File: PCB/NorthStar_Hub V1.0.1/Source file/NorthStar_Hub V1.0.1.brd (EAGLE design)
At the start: 67 x 37 mm, 187 parts, among them IC1 GL3520-OS322, IC2 ATMEGA32U4-MUR, J1 FH34SRJ-6S-0.5SH(50), J10 NA, J3 FH34SRJ-12S-0.5SH(50), J4 XH-2AW, J5 53398-02, J6 SM04B-SRSS-TB, J9 FH34SRJ-12S-0.5SH(50), K1 SKRKAEE020, Q1 CJ2301 S1, Q2 DTC143ZUA, U1 AT25DF512C-MAHN-T, U2 HD3SS3220IRNHR, U3 GL3224E, U4 SY8089, U5 SY8089, U6 TPS2065C, U7 TPS2065C, U8 TPS2065C, X1 16MHZ, X3 25MHZ, X4 25MHZ

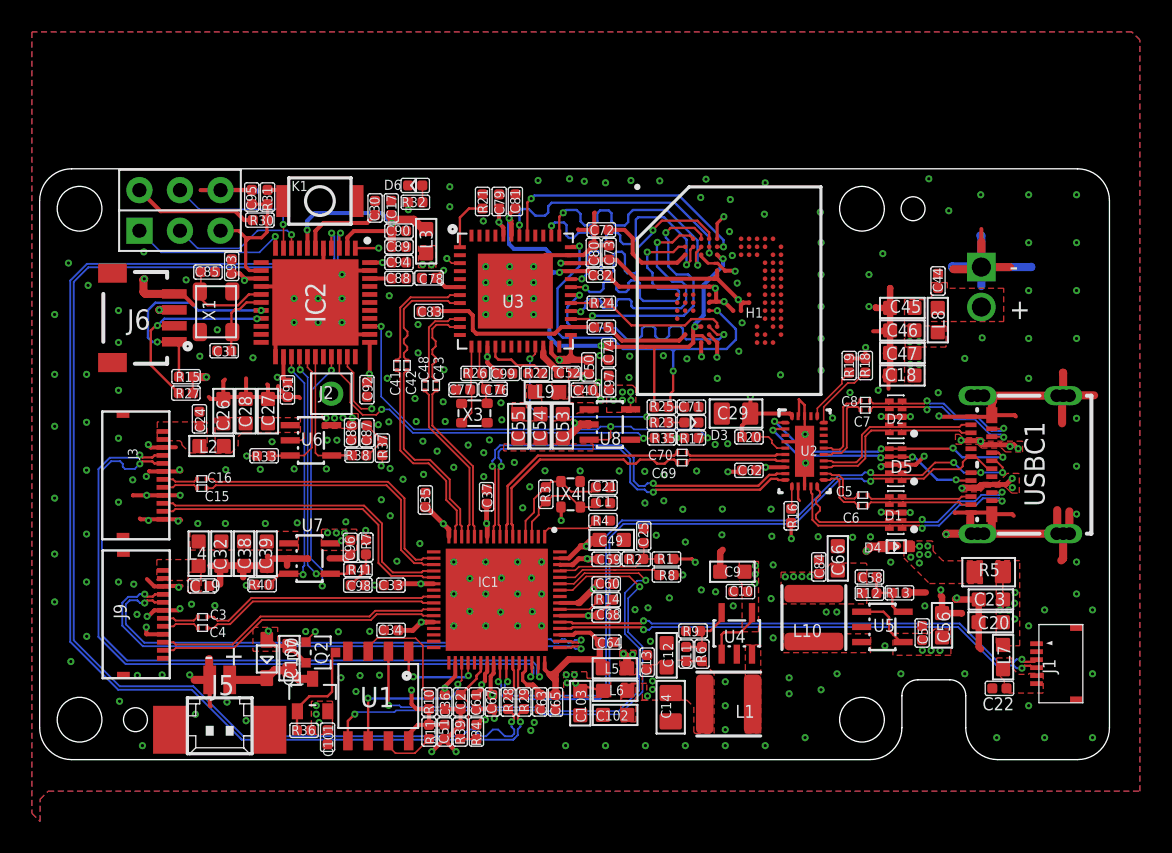
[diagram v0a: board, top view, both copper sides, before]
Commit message: reassign INT to PE6
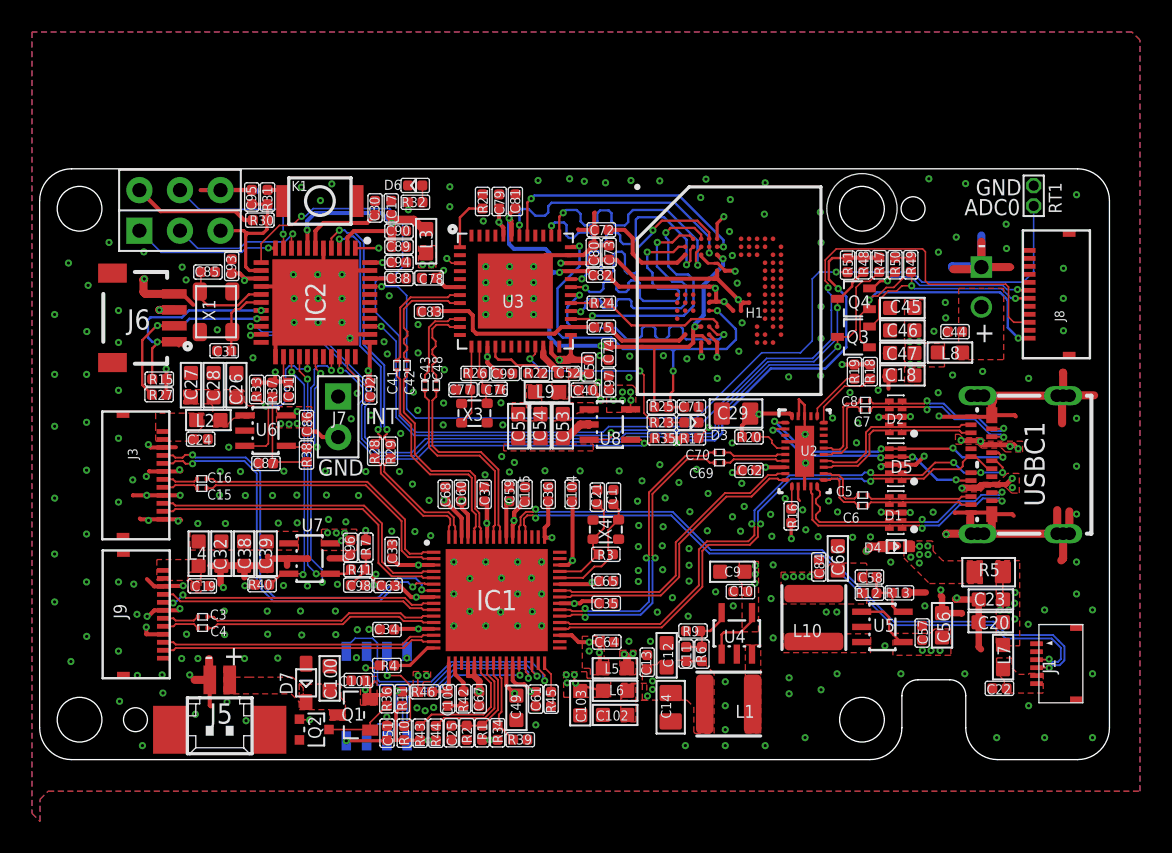
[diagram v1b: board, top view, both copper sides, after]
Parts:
- removed C2: 1uF ±10% 10V, RCL:C0402
- removed J2: (no value), Connector_NOA:1P-60/32MIL
- removed R14: 100K ±1%, RCL:R0402
- removed R8: 10K ±1%, RCL:R0402
- added C104, C105, C106: 100nF ±10% 10V, RCL:C0402
- added J7: 2.54MM 单排正弯针 1*2P PA6.0, Connector_NOA:2P-2.54-65/35MIL
- added J8: FH34SRJ-12S-0.5SH(50), Connector_NOA:FPC-0.5-12P
- added Q3, Q4: BSS138W, Discrete_NOA:SOT-323
- added R42, R46: 0R ±1%, RCL:R0402
- added R43, R44, R45: 10K ±1%, RCL:R0402
- added R47, R48, R49, R50, R51: 4.7K ±1%, RCL:R0402
- added RT1: MF52B 103F3950-100mm, Connector_NOA:2P-1.27
- D7: value PMEG2010AEB,115 -> PMEG2010EA,115
- IC1: value GL3520-OS322 -> GL3510
- R4: value 680R ±1% -> 20K ±1%
- USBC1: value TYPEC-105450-0101105450-0101_USB-C-SMD_TYPE-C-USB-18 -> 1054500101
- moved R28 17.8 mm to (82.0, 125.9), turned to 90 degrees
- moved R29 17.8 mm to (83.0, 125.9), turned to 90 degrees
- moved C25 17.2 mm to (86.8, 108.3), turned to 270 degrees
- moved R4 16.3 mm to (82.8, 112.5), turned to 0 degrees
- moved R1 15.9 mm to (88.8, 108.3), turned to 90 degrees
- moved R2 15.2 mm to (87.8, 108.3), turned to 270 degrees
- moved C36 14.5 mm to (92.9, 123.2), turned to 90 degrees
- moved C35 13.0 mm to (96.5, 116.4), turned to 0 degrees
- moved C68 12.6 mm to (86.5, 123.2), turned to 90 degrees
- moved C49 12.1 mm to (90.9, 109.9), turned to 270 degrees
- moved C63 12.0 mm to (82.9, 117.5), turned to 180 degrees
- moved C60 10.7 mm to (87.5, 123.2), turned to 90 degrees
- moved C65 8.21 mm to (96.5, 117.8), turned to 0 degrees
- moved R37 7.79 mm to (75.6, 129.8), turned to 90 degrees
- moved C59 7.31 mm to (90.5, 123.2), turned to 90 degrees
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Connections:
- net DS1_RX_N renamed DS2_RX_N
- net DS1_RX_P renamed DS2_RX_P
- net DS3TXE_N renamed DS4TXE_N
- net DS3TXE_P renamed DS4TXE_P
- net USB3TX_N renamed USB3TXE_N
- net USB3TX_P renamed USB3TXE_P
- removed net CSBU1: USBC1.A8
- removed net CSBU2: USBC1.B8
- removed net DS1RX_N: C41.1, IC1.15
- removed net DS1RX_P: C42.1, IC1.14
- removed net DS1TXE_N: C48.2, IC1.13
- removed net DS1TXE_P: C43.2, IC1.12
- removed net DS1TX_N: C48.1, U3.10
- removed net DS1TX_P: C43.1, U3.11
- removed net DS1_USB2_N: IC1.43, R28.1
- removed net DS1_USB2_P: IC1.44, R29.1
- removed net DS2_USB2_N: IC1.46, J3.4
- removed net DS2_USB2_P: IC1.47, J3.5
- removed net DS3_USB2_N: IC1.49, J9.4
- removed net DS3_USB2_P: IC1.50, J9.5
- removed net DS4_USB2_N: IC1.52, J1.4
- removed net DS4_USB2_P: IC1.53, J1.3
- removed net N$27: C2.2, IC1.38, R34.1, R39.2
- removed net N$8: IC1.1, R4.2
- removed net PGANG: IC1.55, R14.1
- removed net USB3_DS2RX_N: IC1.20, J3.10
- removed net USB3_DS2RX_P: IC1.21, J3.11
- removed net USB3_DS2TXE_N: C16.1, IC1.18
- removed net USB3_DS2TXE_P: C15.1, IC1.19
- new net +1V8: J8.1, Q3.1, Q4.1, R49.1, R50.1
- new net ANX_I2C_SCL: J8.9
- new net ANX_I2C_SDA: J8.11
- new net ANX_INTP: J8.12
- new net DS1D_N: IC1.53, J1.4
- new net DS1D_P: IC1.52, J1.3
- new net DS2D_N: IC1.64, R28.1
- new net DS2D_P: IC1.63, R29.1
- new net DS2RX_N: C41.1, IC1.60
- new net DS2RX_P: C42.1, IC1.59
- new net DS2TX_N: C48.2, IC1.56
- new net DS2TX_P: C43.2, IC1.57
- new net DS2_TX_N: C43.1, U3.10
- new net DS2_TX_P: C48.1, U3.11
- new net DS3D_N: IC1.7, J3.4
- new net DS3D_P: IC1.6, J3.5
- new net DS4D_N: IC1.10, J9.4
- new net DS4D_P: IC1.9, J9.5
- new net DS4RX_N: IC1.14, J9.10
- new net DS4RX_P: IC1.15, J9.11
- new net DS4TX_N: C3.1, IC1.11
- new net DS4TX_P: C4.1, IC1.12
- new net FN_A: IC1.22, R43.2
- new net FN_B: IC1.23, R44.2
- new net MCU_EXT2_TX: J8.7, Q4.2, R50.2
- new net MCU_EXT3_RX: J8.6, Q3.2, R49.2
- new net MCU_SWD_CLK: J8.4
- new net MCU_SWD_IO: J8.5
- new net MCU_SWD_RST: IC2.12, J8.3
- new net PLED/FN_C: IC1.32, R45.2
- new net RTERM: IC1.16, R4.2
- new net TEMP: IC2.41, R51.2, RT1.1
- new net UART_RX: IC2.20, Q4.3, R48.2
- new net UART_TX: IC2.21, Q3.3, R47.2
- new net VBUS_IN: IC1.25, R34.1, R39.2
- new net VSSP: IC1.18, R42.2
- net +1V2: now also IC1.27, IC1.55, IC1.61, R46.1; no longer IC1.39, IC1.56, IC1.62
- net +3V3: now also IC1.20, IC1.21, IC1.26, IC1.62, R43.1, R44.1, R47.1, R48.1, R51.1; no longer IC1.40, IC1.54, IC1.63, R14.2, R8.2
- net AV12: now also C104.1, IC1.13, IC1.3, IC1.40, IC1.46, IC1.49, IC1.58; no longer IC1.10, IC1.16, IC1.22, IC1.28, IC1.34
- net AV33: now also C105.1, IC1.35, IC1.43, IC1.54, IC1.8; no longer IC1.45, IC1.48, IC1.51
- net DS3RX_N: now also IC1.4, J3.10; no longer IC1.26, J9.10
- net DS3RX_P: now also IC1.5, J3.11; no longer IC1.27, J9.11
- net DS3TX_N: now also C16.1, IC1.1; no longer C3.1, IC1.24
- net DS3TX_P: now also C15.1, IC1.2; no longer C4.1, IC1.25
- net D_UP_N: now also IC1.36; no longer IC1.41
- net D_UP_P: now also IC1.37; no longer IC1.42
- net GND: now also C104.2, C105.2, C106.2, J7.2, J8.10, J8.2, J8.8, R42.1, R45.1, RT1.2; no longer C2.1
- net INT: now also J7.1; no longer J2.P$1
- net N$1: now also IC1.44; no longer IC1.3
- net N$2: now also C106.1, IC1.17, R46.2; no longer C21.1, IC1.4, R3.2, X4.2
- net N$3: now also C21.1, IC1.45, R3.2, X4.2; no longer IC1.60, R8.1
- net RESETJ: now also IC1.24; no longer IC1.61
- net RX_UP_N: now also IC1.41; no longer IC1.8
- net RX_UP_P: now also IC1.42; no longer IC1.9
- net SPI_CK: now also IC1.29; no longer IC1.35
- net SPI_CZ: now also IC1.31; no longer IC1.36
- net SPI_DI: now also IC1.30; no longer IC1.59
- net SPI_DO: now also IC1.28; no longer IC1.58
- net TXUP_N: now also IC1.38; no longer IC1.6
- net TXUP_P: now also IC1.39; no longer IC1.7
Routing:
- net MCU_SWD_RST: track 0.00 -> 77.4 mm, vias 0 -> 2
- net TEMP: track 0.00 -> 60.7 mm, vias 0 -> 2
- net D_N: track 75.0 -> 15.5 mm
- net D_P: track 75.0 -> 16.7 mm
- net UART_TX: track 0.00 -> 52.9 mm, vias 0 -> 2
- net UART_RX: track 0.00 -> 51.5 mm, vias 0 -> 2
- net DS2_USB2_P: track 44.6 -> 0.00 mm, vias 2 -> 0
- net DS2_USB2_N: track 44.6 -> 0.00 mm, vias 2 -> 0
- net DS1D_N: track 0.00 -> 42.2 mm, vias 0 -> 2
- net DS1D_P: track 0.00 -> 40.9 mm, vias 0 -> 2
- net DS3_USB2_N: track 35.1 -> 0.00 mm, vias 2 -> 0
- net DS3_USB2_P: track 35.1 -> 0.00 mm, vias 2 -> 0
- net GND: track 211.2 -> 179.8 mm, vias 289 -> 324
- net DS4_USB2_P: track 31.2 -> 0.00 mm, vias 2 -> 0
- net DS4_USB2_N: track 31.2 -> 0.00 mm, vias 2 -> 0
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- added copper zone on layer 1, net AV33
- added copper zone on layer 15, net AV33
- added copper zone on layer 1, net N$24
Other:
- board text added: "ADC0"
- board text added: "GND"
- board text added: "INT GND"
- board text added: "NorthStar_Hub_V1.0.1"
- board text removed: "NorthStar_Hub_V0.3.1 20200717"
